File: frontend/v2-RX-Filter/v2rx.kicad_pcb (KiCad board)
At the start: 2 copper layers, 100 x 100 mm, 192 parts, among them K1 D3002, K2 D3002, K3 D3002, K4 D3002, K5 D3002, K6 D3002, K7 D3002, P1 CONN_01X02, P3 External 12V-13.8V (OSTTC0221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, P4 CONN_01X02, P5 CONN_01X02, P6 TX Filter Activate Jumper, P7 Control from MegaBasic, Q2 FDV301, Q3 RD16HHF1, Q4 FDV301, T2 OUT_TRANSF, U2 74LS145, U3 74LS145, U6 LP2951-50D

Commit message: Latest Rx updates
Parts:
- removed C83: 1000pF, HERMESLITE:C_0805
- removed C84, C85: 0.01uF, HERMESLITE:C_0805
- removed C86: 150pF, HERMESLITE:C_0805
- removed C87, C96: 1uF, HERMESLITE:C_0805
- removed C88, C89, C90, C91, C92: 0.1uF, HERMESLITE:C_0805
- removed D1, D10, D11, D12, D13, D14, D15, D16, D17, D2, D3, D4, D5, D6, D7, D8, D9: DIODE, Diodes_SMD:Diode-SMA_Standard
- removed D18: RED LED (PTT), LEDs:LED-0805
- removed K1, K2, K3, K4, K5, K6, K7: D3002, HERMESLITE:D3002
- removed L22, L32: 2.7uH, HERMESLITE:Choke_SMD_1206_Standard
- removed L23, L24, L33: 4.7uH, HERMESLITE:Choke_SMD_1206_Standard
- removed L25: 100nH, HERMESLITE:Choke_SMD_1206_Standard
- removed L26: 150nH, HERMESLITE:Choke_SMD_1206_Standard
- removed L27: 330nH, HERMESLITE:Choke_SMD_1206_Standard
- removed L28, L36: 680nH, HERMESLITE:Choke_SMD_1206_Standard
- removed L29, L37: 1.5uH, HERMESLITE:Choke_SMD_1206_Standard
- removed L30: 1uH, HERMESLITE:Choke_SMD_1206_Standard
- removed L31: 1.8uH, HERMESLITE:Choke_SMD_1206_Standard
- removed L34: 270nH, HERMESLITE:Choke_SMD_1206_Standard
- removed L35: 390nH, HERMESLITE:Choke_SMD_1206_Standard
- removed L38, L39, L40: 4700nH, HERMESLITE:Choke_SMD_1206_Standard
- removed the MH at (104.1, 53.9)
- removed the MH at (146.6, 53.8)
- removed the MH at (104.0, 92.4)
- removed the MH at (145.8, 83.4)
- removed the MH at (196.0, 54.0)
- removed the MH at (196.2, 146.2)
- removed the MH at (104.0, 146.1)
- removed MountingHole_6mm: VAL**, Mounting_Holes:MountingHole_6mm
- removed P6: TX Filter Activate Jumper, Pin_Headers:Pin_Header_Straight_1x02
- removed P7: Control from MegaBasic, Pin_Headers:Pin_Header_Straight_1x07
- removed Q2, Q4: FDV301, HERMESLITE:SOT-23-GDS
- removed Q3: RD16HHF1, Transistors_TO-220:TO-220_Neutral123_Vertical_LargePads
- removed R10: 270, HERMESLITE:R_0805
- removed R13, R14, R15, R16, R17, R18, R19: 1k, HERMESLITE:R_0805
- removed R2: 4.99k, HERMESLITE:R_0805
- removed R20, R21: 270 1W, Resistors_ThroughHole:Resistor_Vertical_RM5mm
- removed R5: 6.8, HERMESLITE:R_0805
- removed R6: 10k, HERMESLITE:R_0805
- removed T2: OUT_TRANSF, HERMESLITE:OUT_TRANSF
- removed VR1: 1k MT, Potentiometers:Potentiometer_Bourns_3296W_3-8Zoll_Inline_ScrewUp
- added C5: DNI, HERMESLITE:C_0805, F.Cu at (144.8, 136.5)
- added FB1: BLM21PG220SN1D, Resistors_SMD:R_0805_HandSoldering, F.Cu at (234.3, 129.4)
- added FB2: BLM21PG220SN1D, Resistors_SMD:R_0805_HandSoldering, F.Cu at (232.4, 140.5)
- added MH: VAL**, HERMESLITE:MH, F.Cu at (185.6, 45.0)
- added MH: VAL**, HERMESLITE:MH, F.Cu at (113.9, 45.0)
- added MH: VAL**, HERMESLITE:MH, F.Cu at (114.2, 136.2)
- added MH: VAL**, HERMESLITE:MH, F.Cu at (185.4, 136.4)
- added P2: CONN_01X02, Pin_Headers:Pin_Header_Straight_1x02, F.Cu at (205.0, 75.4)
- added U1: 4504, Housings_SOIC:SOIC-16_3.9x9.9mm_Pitch1.27mm, F.Cu at (94.7, 90.6)
- added U10: PE4259-53, HERMESLITE:sc70-6, F.Cu at (179.1, 49.8)
- added U11: PE4259-53, HERMESLITE:sc70-6, F.Cu at (178.0, 61.9)
- added U12: PE4259-53, HERMESLITE:sc70-6, F.Cu at (179.1, 76.4)
- added U13: PE4259-53, HERMESLITE:sc70-6, F.Cu at (207.8, 119.1)
- added U14: PE4259-53, HERMESLITE:sc70-6, F.Cu at (208.0, 124.7)
- added U15: PE4259-53, HERMESLITE:sc70-6, F.Cu at (208.3, 130.4)
- added U16: PE4259-53, HERMESLITE:sc70-6, F.Cu at (208.5, 136.2)
- added U4: PE4259-53, HERMESLITE:sc70-6, F.Cu at (140.1, 77.2)
- added U5: PE4259-53, HERMESLITE:sc70-6, F.Cu at (196.0, 120.5)
- added U7: PE4259-53, HERMESLITE:sc70-6, F.Cu at (196.5, 132.0)
- added U8: PE4259-53, HERMESLITE:sc70-6, F.Cu at (196.5, 137.1)
- added U9: 4504, Housings_SOIC:SOIC-16_3.9x9.9mm_Pitch1.27mm, F.Cu at (85.2, 103.8)
- C10: value 10uF 16V -> DNI; footprint Capacitors_Tantalum_SMD:TantalC_SizeB_EIA-3528_Reflow -> HERMESLITE:C_0805; moved to F.Cu
- C11: value 4700pF -> DNI; moved to F.Cu
- C12, C13: value 120pF -> DNI; moved to F.Cu
- C14: value 82pF -> DNI; moved to F.Cu
- C15, C24, C36, C38: value 150pF -> DNI; moved to F.Cu
- C16: value 150pF -> 68pF; moved to F.Cu
- C17: value 470pF -> DNI; moved to F.Cu
- C18: value 150pF -> 120pF; moved to F.Cu
- C19, C25: value 150pF -> 180pF; moved to F.Cu
- C2: value 47uF 16V -> DNI; footprint Capacitors_Tantalum_SMD:TantalC_SizeD_EIA-7343_Reflow -> HERMESLITE:C_0805; moved to F.Cu
- C20, C26: value 1800pF -> 330pF; moved to F.Cu
- C21: value DNI -> 560pF; moved to F.Cu
- C22: value DNI -> 1000pF; moved to F.Cu
- C23: value DNI -> 120pF; moved to F.Cu
- C27: value 270pF -> 560pF; moved to F.Cu
- C28: value 560pF -> 1200pF; moved to F.Cu
- C29: value 1000pF -> 1500pF; moved to F.Cu
- C3, C6: value 0.1uF -> DNI
- C30: value 3300pF -> DNI; moved to F.Cu
- C31: value 560pF -> DNI; moved to F.Cu
- C32, C33, C34: moved to F.Cu
- C35: value 220pF -> DNI; moved to F.Cu
- C37: value 3300pF -> 120pF; moved to F.Cu
- C39: value 150pF -> 270pF; moved to F.Cu
- C4, C7, C8: value 0.1uF -> DNI; moved to F.Cu
- C40: value 470pF -> 270pF; moved to F.Cu
- C41: value 150pF -> 680pF; moved to F.Cu
- C42: value 150pF -> 1200pF; moved to F.Cu
- C43: value 0.1uF -> 1500pF
- C45: value 0.01uF -> 120pF
- C46, C59, C69, C70, C71, C72: value 0.01uF -> DNI
- C47: value 0.01uF -> 180pF
- C48: value 0.01uF -> 330pF
- C49: value 100pF -> 560pF
- C50: value 270pF -> 1200pF
- C51: value 560pF -> 1500pF
- C52: value 1000pF -> 0.1uF
- C53: value 1000pF -> DNI
- C54: value 39pF -> DNI
- C55: value 56pF -> DNI
- C56, C57, C58, C67, C68, C73: value 150pF -> DNI
- C60: value 390pF -> 68pF
- C61: value 680pF -> DNI
- C62: value 1200pF -> 120pF
- C63: value 2200pF -> 180pF
- C64: value 1000pF -> 330pF
- C65: value 39pF -> 560pF
- C66: value 56pF -> 1000pF
- C74: value 270pF -> 0.1uF
- C75: value 560pF -> 0.01uF
- C76: value 1000pF -> 0.01uF
- C77, C82: value 0.1uF -> 0.01uF
- C78, C79: value 150pF -> 0.01uF
- C80, C81: value 150pF -> 0.1uF; moved to F.Cu
- C9: value 1uF -> DNI; moved to F.Cu
- L1: value FT37-43 11T #26 -> 680nH; footprint Choke_Axial_ThroughHole:Choke_Horizontal_RM10mm -> HERMESLITE:inductor
- L10: value 300nH -> 820nH; footprint Choke_Toroid_ThroughHole:Choke_Toroid_6,5x13mm_Vertical -> HERMESLITE:inductor
- L11: value 430nH -> 1.5uH; footprint Choke_Toroid_ThroughHole:Choke_Toroid_6,5x13mm_Vertical -> HERMESLITE:inductor
- L12: value 2.92uH -> 2.2uH; footprint Choke_Toroid_ThroughHole:Choke_Toroid_6,5x13mm_Vertical -> HERMESLITE:inductor
- L13: value 1.02uH -> 3.9uH; footprint Choke_Toroid_ThroughHole:Choke_Toroid_6,5x13mm_Vertical -> HERMESLITE:inductor
- L14: value 4700nH -> 8.2uH; footprint HERMESLITE:Choke_SMD_1206_Standard -> HERMESLITE:inductor
- L15: value 270nH -> 680nH; footprint HERMESLITE:Choke_SMD_1206_Standard -> HERMESLITE:inductor
- L16: value 390nH -> DNI; footprint HERMESLITE:Choke_SMD_1206_Standard -> HERMESLITE:inductor
- L17: value 680nH -> 820nH; footprint HERMESLITE:Choke_SMD_1206_Standard -> HERMESLITE:inductor
- L18: footprint HERMESLITE:Choke_SMD_1206_Standard -> HERMESLITE:inductor
- L19: value 1.5uH -> 2.2uH; footprint HERMESLITE:Choke_SMD_1206_Standard -> HERMESLITE:inductor
- L2: value 192nH -> DNI; footprint Choke_Toroid_ThroughHole:Choke_Toroid_6,5x13mm_Vertical -> HERMESLITE:inductor
- L20: value 1uH -> 3.9uH; footprint HERMESLITE:Choke_SMD_1206_Standard -> HERMESLITE:inductor
- L21: value 1.8uH -> 8.2uH; footprint HERMESLITE:Choke_SMD_1206_Standard -> HERMESLITE:inductor
- L3: value 192nH -> 820nH; footprint Choke_Toroid_ThroughHole:Choke_Toroid_6,5x13mm_Vertical -> HERMESLITE:inductor
- L4: value 240nH -> 1.5uH; footprint Choke_Toroid_ThroughHole:Choke_Toroid_6,5x13mm_Vertical -> HERMESLITE:inductor
- L5: value 300nH -> 2.2uH; footprint Choke_Toroid_ThroughHole:Choke_Toroid_6,5x13mm_Vertical -> HERMESLITE:inductor
- L6: value 430nH -> 3.9uH; footprint Choke_Toroid_ThroughHole:Choke_Toroid_6,5x13mm_Vertical -> HERMESLITE:inductor
- L7: value 1.44uH -> 8.2uH; footprint Choke_Toroid_ThroughHole:Choke_Toroid_6,5x13mm_Vertical -> HERMESLITE:inductor
- L8: value 1.02uH -> 680nH; footprint Choke_Toroid_ThroughHole:Choke_Toroid_6,5x13mm_Vertical -> HERMESLITE:inductor
- L9: value 240nH -> DNI; footprint Choke_Toroid_ThroughHole:Choke_Toroid_6,5x13mm_Vertical -> HERMESLITE:inductor
- P1: value CONN_01X02 -> CONN_02X07; footprint Pin_Headers:Pin_Header_Straight_1x02 -> Pin_Headers:Pin_Header_Straight_2x07
- P3: value External 12V-13.8V (OSTTC022162) -> CONN_02X03; footprint Connect:AK300-2 -> Pin_Headers:Pin_Header_Straight_2x03
- P4: value CONN_01X02 -> CONN_02X03; footprint Pin_Headers:Pin_Header_Straight_1x02 -> Pin_Headers:Pin_Header_Straight_2x03
- U2, U3: value 74LS145 -> PE4259-53; footprint Housings_SOIC:SOIC-16_3.9x9.9mm_Pitch1.27mm -> HERMESLITE:sc70-6
- U6: value LP2951-50D -> PE4259-53; footprint Housings_SOIC:SOIC-8_3.9x4.9mm_Pitch1.27mm -> HERMESLITE:sc70-6; moved to F.Cu
- moved C53 102.0 mm to (165.0, 49.0), turned to 270 degrees
- moved C27 90.7 mm to (121.9, 122.6), turned to 0 degrees
- moved C29 88.5 mm to (109.1, 131.4), turned to 0 degrees
- moved C33 88.5 mm to (119.4, 128.3), turned to 0 degrees
- moved C11 83.5 mm to (130.0, 143.1), turned to 0 degrees
- moved C42 82.2 mm to (109.3, 141.5), turned to 0 degrees
- moved P4 79.6 mm to (185.3, 53.4), turned to 270 degrees
- moved L4 79.4 mm to (126.2, 107.8), turned to 0 degrees
- moved C4 79.2 mm to (160.1, 136.0)
- moved L8 78.6 mm to (157.5, 51.3), turned to 0 degrees
- moved C30 77.5 mm to (157.9, 55.6), turned to 180 degrees
- moved C67 76.6 mm to (175.6, 53.8), turned to 270 degrees
- moved C8 76.3 mm to (141.9, 138.7), turned to 0 degrees
- moved C45 76.0 mm to (171.4, 56.1)
- moved C37 75.5 mm to (163.8, 52.8), turned to 180 degrees
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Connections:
- C1 pad 1: +12V -> Net-(C1-Pad1)
- C1 pad 2: GND -> Net-(C1-Pad2)
- C10 pad 2: GND -> Net-(C10-Pad2)
- C11 pad 1: GND -> Net-(C11-Pad1)
- C11 pad 2: Net-(C10-Pad1) -> Net-(C11-Pad2)
- C12 pad 2: GND -> Net-(C12-Pad2)
- C13 pad 2: GND -> Net-(C13-Pad2)
- C14 pad 1: TXIN -> Net-(C14-Pad1)
- C14 pad 2: GND -> Net-(C14-Pad2)
- C15 pad 2: GND -> Net-(C15-Pad2)
- C16 pad 2: GND -> Net-(C16-Pad2)
- C17 pad 2: GND -> Net-(C10-Pad1)
- C18 pad 2: GND -> Net-(C11-Pad1)
- C19 pad 1: Net-(C18-Pad1) -> Net-(C19-Pad1)
- C19 pad 2: GND -> Net-(C12-Pad1)
- C2 pad 1: +12V -> Net-(C2-Pad1)
- C20 pad 2: GND -> Net-(C13-Pad1)
- C21 pad 1: Net-(C15-Pad1) -> Net-(C21-Pad1)
- C21 pad 2: Net-(C21-Pad2) -> Net-(C14-Pad1)
- C22 pad 1: Net-(C16-Pad1) -> Net-(C22-Pad1)
- C22 pad 2: Net-(C22-Pad2) -> Net-(C15-Pad1)
- C23 pad 1: Net-(C17-Pad1) -> Net-(C16-Pad1)
- C23 pad 2: Net-(C23-Pad2) -> GND
- C24 pad 1: Net-(C24-Pad1) -> Net-(C17-Pad1)
- C24 pad 2: Net-(C20-Pad1) -> GND
- C25 pad 2: Net-(C25-Pad2) -> GND
- C26 pad 1: Net-(C24-Pad1) -> Net-(C19-Pad1)
- C27 pad 1: Net-(C21-Pad2) -> Net-(C20-Pad1)
- C28 pad 1: Net-(C22-Pad2) -> Net-(C21-Pad1)
- C29 pad 1: Net-(C23-Pad2) -> Net-(C22-Pad1)
- C3 pad 1: Net-(C3-Pad1) -> Net-(C10-Pad2)
- C3 pad 2: Net-(C3-Pad2) -> GND
- C30 pad 2: GND -> Net-(C16-Pad1)
- C31 pad 1: Net-(C25-Pad2) -> Net-(C31-Pad1)
- C31 pad 2: GND -> Net-(C17-Pad1)
- C32 pad 1: Net-(C21-Pad2) -> Net-(C32-Pad1)
- C32 pad 2: Net-(C32-Pad2) -> Net-(C18-Pad1)
- C33 pad 1: Net-(C22-Pad2) -> Net-(C33-Pad1)
- C33 pad 2: Net-(C33-Pad2) -> Net-(C19-Pad1)
- C34 pad 1: Net-(C23-Pad2) -> Net-(C34-Pad1)
- C34 pad 2: Net-(C34-Pad2) -> Net-(C20-Pad1)
- C35 pad 2: Net-(C30-Pad1) -> Net-(C21-Pad1)
- C36 pad 1: Net-(C25-Pad2) -> Net-(C36-Pad1)
- C36 pad 2: Net-(C36-Pad2) -> Net-(C22-Pad1)
- C37 pad 1: Net-(C35-Pad1) -> Net-(C37-Pad1)
- C37 pad 2: GND -> Net-(C30-Pad1)
- C38 pad 1: Net-(C32-Pad2) -> Net-(C38-Pad1)
- C38 pad 2: GND -> Net-(C31-Pad1)
- C39 pad 1: Net-(C33-Pad2) -> Net-(C39-Pad1)
- C39 pad 2: GND -> Net-(C32-Pad1)
- C4 pad 1: Net-(C4-Pad1) -> Net-(C11-Pad2)
- C40 pad 1: Net-(C34-Pad2) -> Net-(C40-Pad1)
- C40 pad 2: GND -> Net-(C33-Pad1)
- C41 pad 1: Net-(C36-Pad2) -> Net-(C41-Pad1)
- C41 pad 2: GND -> Net-(C34-Pad1)
- C42 pad 1: Net-(C36-Pad2) -> Net-(C42-Pad1)
- C42 pad 2: GND -> Net-(C35-Pad1)
- C43 pad 2: RX-OUT -> Net-(C36-Pad1)
- C44 pad 1: Net-(C44-Pad1) -> GND
- C44 pad 2: GND -> Net-(C44-Pad2)
- C45 pad 1: Net-(C45-Pad1) -> Net-(C37-Pad1)
- C46 pad 1: Net-(C46-Pad1) -> Net-(C38-Pad1)
- C47 pad 1: Net-(C47-Pad1) -> Net-(C39-Pad1)
- C48 pad 1: Net-(C48-Pad1) -> Net-(C40-Pad1)
- C49 pad 1: Net-(C49-Pad1) -> Net-(C41-Pad1)
- C50 pad 1: Net-(C50-Pad1) -> Net-(C42-Pad1)
- C51 pad 1: Net-(C51-Pad1) -> Net-(C43-Pad1)
- C53 pad 2: GND -> Net-(C37-Pad1)
- C54 pad 2: Net-(C54-Pad2) -> Net-(C38-Pad1)
- C55 pad 2: Net-(C55-Pad2) -> Net-(C39-Pad1)
- C56 pad 2: Net-(C56-Pad2) -> Net-(C40-Pad1)
- C57 pad 2: Net-(C57-Pad2) -> Net-(C41-Pad1)
- C58 pad 2: Net-(C58-Pad2) -> Net-(C42-Pad1)
- C59 pad 1: Net-(C48-Pad1) -> Net-(C59-Pad1)
- C59 pad 2: GND -> Net-(C43-Pad1)
- C6 pad 1: Net-(C6-Pad1) -> Net-(C13-Pad2)
- C6 pad 2: Net-(C6-Pad2) -> GND
- C60 pad 1: Net-(C54-Pad1) -> Net-(C60-Pad1)
- C60 pad 2: GND -> Net-(C53-Pad1)
- C61 pad 1: Net-(C55-Pad1) -> Net-(C61-Pad1)
- C61 pad 2: GND -> Net-(C54-Pad1)
- C62 pad 1: Net-(C56-Pad1) -> Net-(C62-Pad1)
- C62 pad 2: GND -> Net-(C55-Pad1)
- C63 pad 1: Net-(C57-Pad1) -> Net-(C63-Pad1)
- C63 pad 2: GND -> Net-(C56-Pad1)
- C64 pad 1: Net-(C58-Pad1) -> Net-(C64-Pad1)
- C64 pad 2: GND -> Net-(C57-Pad1)
- C65 pad 2: Net-(C65-Pad2) -> Net-(C58-Pad1)
- C66 pad 2: Net-(C66-Pad2) -> Net-(C59-Pad1)
- C67 pad 1: Net-(C67-Pad1) -> Net-(C60-Pad1)
- C67 pad 2: Net-(C67-Pad2) -> GND
- C68 pad 1: Net-(C68-Pad1) -> Net-(C61-Pad1)
- C68 pad 2: Net-(C68-Pad2) -> GND
- C69 pad 1: Net-(C44-Pad1) -> Net-(C62-Pad1)
- C7 pad 1: GND -> Net-(C14-Pad2)
- C7 pad 2: Net-(C10-Pad1) -> GND
- C70 pad 1: Net-(C45-Pad1) -> Net-(C63-Pad1)
- C71 pad 1: Net-(C46-Pad1) -> Net-(C64-Pad1)
- C72 pad 1: Net-(C47-Pad1) -> Net-(C65-Pad1)
- C73 pad 1: Net-(C65-Pad1) -> Net-(C66-Pad1)
- C74 pad 1: Net-(C66-Pad1) -> Net-(C74-Pad1)
- C74 pad 2: GND -> Net-(C74-Pad2)
- C75 pad 1: Net-(C67-Pad1) -> GND
- C75 pad 2: GND -> Net-(C75-Pad2)
- C76 pad 1: Net-(C68-Pad1) -> GND
- C76 pad 2: GND -> Net-(C76-Pad2)
- C77 pad 1: RX-IN -> GND
- C78 pad 1: Net-(C57-Pad1) -> GND
- C78 pad 2: Net-(C57-Pad2) -> Net-(C78-Pad2)
- C79 pad 1: Net-(C68-Pad1) -> GND
- C79 pad 2: Net-(C68-Pad2) -> Net-(C79-Pad2)
- C8 pad 1: GND -> Net-(C15-Pad2)
- C8 pad 2: Net-(C10-Pad1) -> GND
- C80 pad 1: Net-(C16-Pad1) -> Net-(C52-Pad1)
- C81 pad 1: Net-(C33-Pad2) -> GND
- C81 pad 2: GND -> Net-(C81-Pad2)
- C82 pad 1: Net-(C82-Pad1) -> GND
- C82 pad 2: TXIN -> Net-(C82-Pad2)
- C9 pad 1: GND -> Net-(C16-Pad2)
- C9 pad 2: Net-(C10-Pad1) -> Net-(C2-Pad1)
- L1 pad 1: +12V -> Net-(C2-Pad1)
- L1 pad 2: Net-(C10-Pad1) -> Net-(C16-Pad2)
- L10 pad 1: Net-(C22-Pad2) -> Net-(C18-Pad1)
- L10 pad 2: Net-(C33-Pad2) -> Net-(C32-Pad1)
- L11 pad 1: Net-(C23-Pad2) -> Net-(C19-Pad1)
- L11 pad 2: Net-(C34-Pad2) -> Net-(C33-Pad1)
- L12 pad 1: Net-(C30-Pad1) -> Net-(C20-Pad1)
- L12 pad 2: Net-(C35-Pad1) -> Net-(C34-Pad1)
- L13 pad 1: Net-(C25-Pad2) -> Net-(C21-Pad1)
- L13 pad 2: Net-(C36-Pad2) -> Net-(C35-Pad1)
- L14 pad 1: Net-(L14-Pad1) -> Net-(C22-Pad1)
- L14 pad 2: Net-(C43-Pad1) -> Net-(C36-Pad1)
- L15 pad 1: Net-(C49-Pad1) -> Net-(C37-Pad1)
- L15 pad 2: Net-(C44-Pad1) -> Net-(C53-Pad1)
- L16 pad 1: Net-(C50-Pad1) -> Net-(C38-Pad1)
- L16 pad 2: Net-(C45-Pad1) -> Net-(C54-Pad1)
- L17 pad 1: Net-(C51-Pad1) -> Net-(C39-Pad1)
- L17 pad 2: Net-(C46-Pad1) -> Net-(C55-Pad1)
- L18 pad 1: Net-(C52-Pad1) -> Net-(C40-Pad1)
- L18 pad 2: Net-(C47-Pad1) -> Net-(C56-Pad1)
- L19 pad 1: Net-(C53-Pad1) -> Net-(C41-Pad1)
- L19 pad 2: Net-(C48-Pad1) -> Net-(C57-Pad1)
- L2 pad 1: Net-(C13-Pad1) -> Net-(C10-Pad2)
- L2 pad 2: Net-(C12-Pad1) -> Net-(C10-Pad1)
- L20 pad 1: Net-(C49-Pad1) -> Net-(C42-Pad1)
- L20 pad 2: Net-(C54-Pad2) -> Net-(C58-Pad1)
- L21 pad 1: Net-(C50-Pad1) -> Net-(C43-Pad1)
- L21 pad 2: Net-(C55-Pad2) -> Net-(C59-Pad1)
- L3 pad 1: TXIN -> Net-(C11-Pad2)
- L3 pad 2: Net-(C13-Pad1) -> Net-(C11-Pad1)
- L4 pad 1: Net-(C15-Pad1) -> Net-(C12-Pad2)
- L4 pad 2: Net-(C21-Pad2) -> Net-(C12-Pad1)
- L5 pad 1: Net-(C16-Pad1) -> Net-(C13-Pad2)
- L5 pad 2: Net-(C22-Pad2) -> Net-(C13-Pad1)
- L6 pad 1: Net-(C17-Pad1) -> Net-(C14-Pad2)
- L6 pad 2: Net-(C23-Pad2) -> Net-(C14-Pad1)
- L7 pad 1: Net-(C20-Pad1) -> Net-(C15-Pad2)
- L7 pad 2: Net-(C24-Pad1) -> Net-(C15-Pad1)
- L8 pad 1: Net-(C18-Pad1) -> Net-(C16-Pad1)
- L8 pad 2: Net-(C25-Pad2) -> Net-(C30-Pad1)
- L9 pad 1: Net-(C21-Pad2) -> Net-(C17-Pad1)
- L9 pad 2: Net-(C32-Pad2) -> Net-(C31-Pad1)
- P1 pad 1: GND -> Net-(P1-Pad1)
- P1 pad 2: Net-(K1-Pad3) -> GND
- P3 pad 1: GND -> Net-(P3-Pad1)
- P3 pad 2: +12V -> GND
- P4 pad 1: GND -> Net-(P4-Pad1)
- P4 pad 2: Net-(C3-Pad2) -> GND
- P5 pad 2: RX-OUT -> Net-(C74-Pad1)
- U2 pad 1: Net-(K7-Pad10) -> Net-(P3-Pad1)
- U2 pad 2: Net-(K6-Pad10) -> GND
- U2 pad 3: Net-(K5-Pad10) -> Net-(P3-Pad5)
- U2 pad 4: Net-(K5-Pad10) -> Net-(C44-Pad2)
- U2 pad 5: Net-(K4-Pad10) -> Net-(C2-Pad1)
- U2 pad 6: Net-(K4-Pad10) -> Net-(C81-Pad2)
- U3 pad 1: Net-(C48-Pad1) -> GND
- U3 pad 2: Net-(C47-Pad1) -> GND
- U3 pad 3: Net-(C47-Pad1) -> Net-(C1-Pad1)
- U3 pad 4: Net-(C46-Pad1) -> Net-(C75-Pad2)
- U3 pad 5: Net-(C46-Pad1) -> Net-(C10-Pad2)
- U3 pad 6: Net-(C45-Pad1) -> Net-(C81-Pad2)
- U6 pad 1: 5V -> GND
- U6 pad 2: 5V -> GND
- U6 pad 3: GND -> Net-(C1-Pad1)
- U6 pad 4: GND -> Net-(C78-Pad2)
- U6 pad 5: Net-(U6-Pad5) -> Net-(C13-Pad2)
- U6 pad 6: Net-(U6-Pad6) -> Net-(C81-Pad2)
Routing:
- net +12V: track 328.3 -> 0.00 mm, vias 10 -> 0
- net GND: track 203.5 -> 23.3 mm, vias 61 -> 9
- net Net-(K2-Pad1): track 117.4 -> 0.00 mm, vias 1 -> 0
- net 5V: track 86.1 -> 0.00 mm, vias 2 -> 0
- net Net-(P7-Pad2): track 85.7 -> 0.00 mm, vias 5 -> 0
- net Net-(C47-Pad1): track 76.3 -> 0.00 mm, vias 4 -> 0
- net Net-(C46-Pad1): track 75.2 -> 0.00 mm, vias 3 -> 0
- net Net-(D1-Pad1): track 75.0 -> 0.00 mm
- net Net-(K1-Pad7): track 72.9 -> 0.00 mm, vias 3 -> 0
- net Net-(C45-Pad1): track 69.7 -> 0.00 mm, vias 2 -> 0
- net Net-(C44-Pad1): track 68.5 -> 0.00 mm, vias 3 -> 0
- net Net-(C48-Pad1): track 68.5 -> 0.00 mm
- net Net-(C81-Pad2): track 0.00 -> 67.1 mm, vias 0 -> 4
- net Net-(K2-Pad10): track 64.4 -> 0.00 mm, vias 2 -> 0
- net Net-(C6-Pad2): track 59.9 -> 0.00 mm
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- removed copper zone on F.Cu, net GND
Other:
- board size 100 x 100 mm -> 80 x 101.2 mm
- board text removed: "+12-14V"
- board text removed: "ANT"
- board text removed: "GND"
- board text removed: "RX"
- board text removed: "Shield"
- board text removed: "TX"

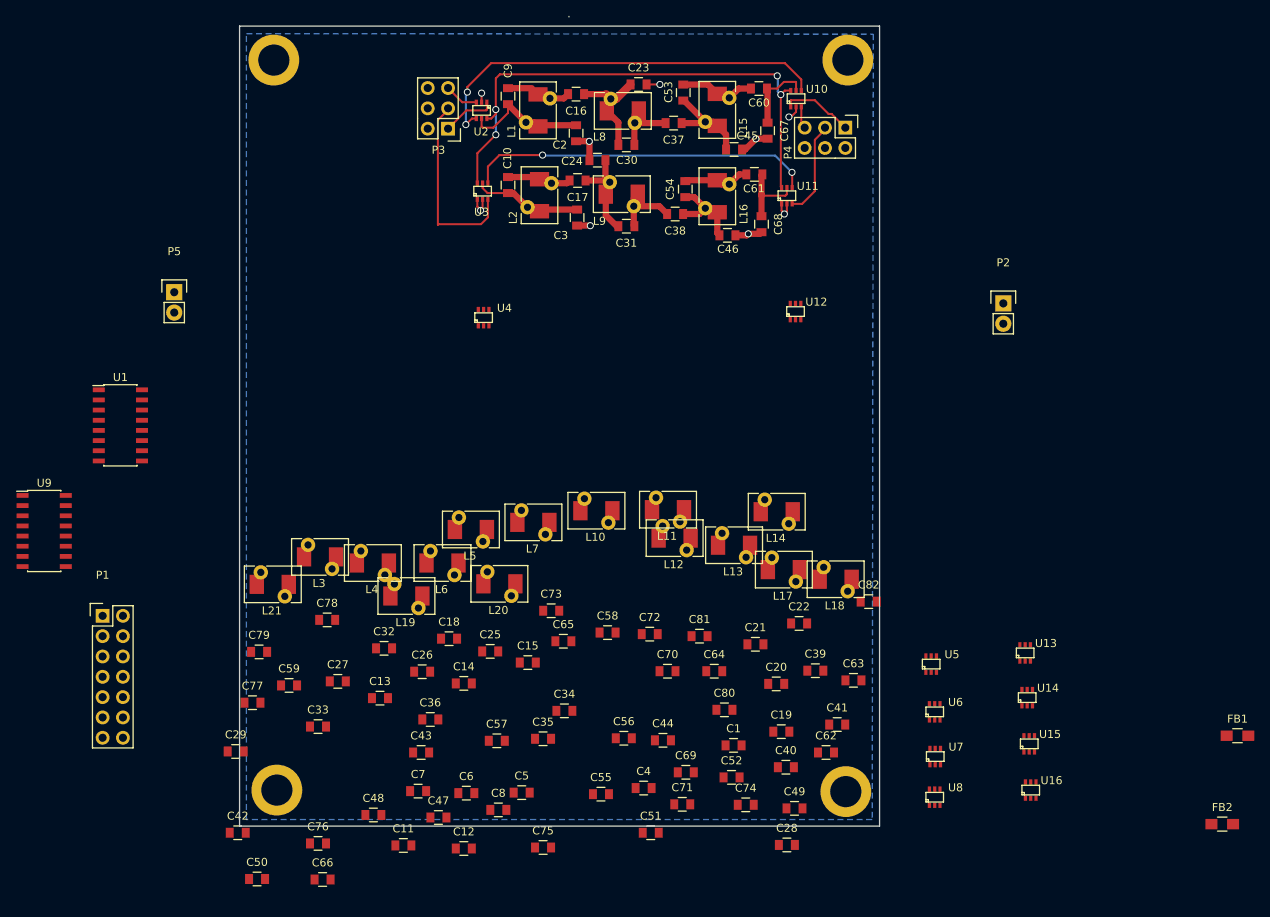
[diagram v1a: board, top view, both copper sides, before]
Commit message: New RX Filter Board Layout
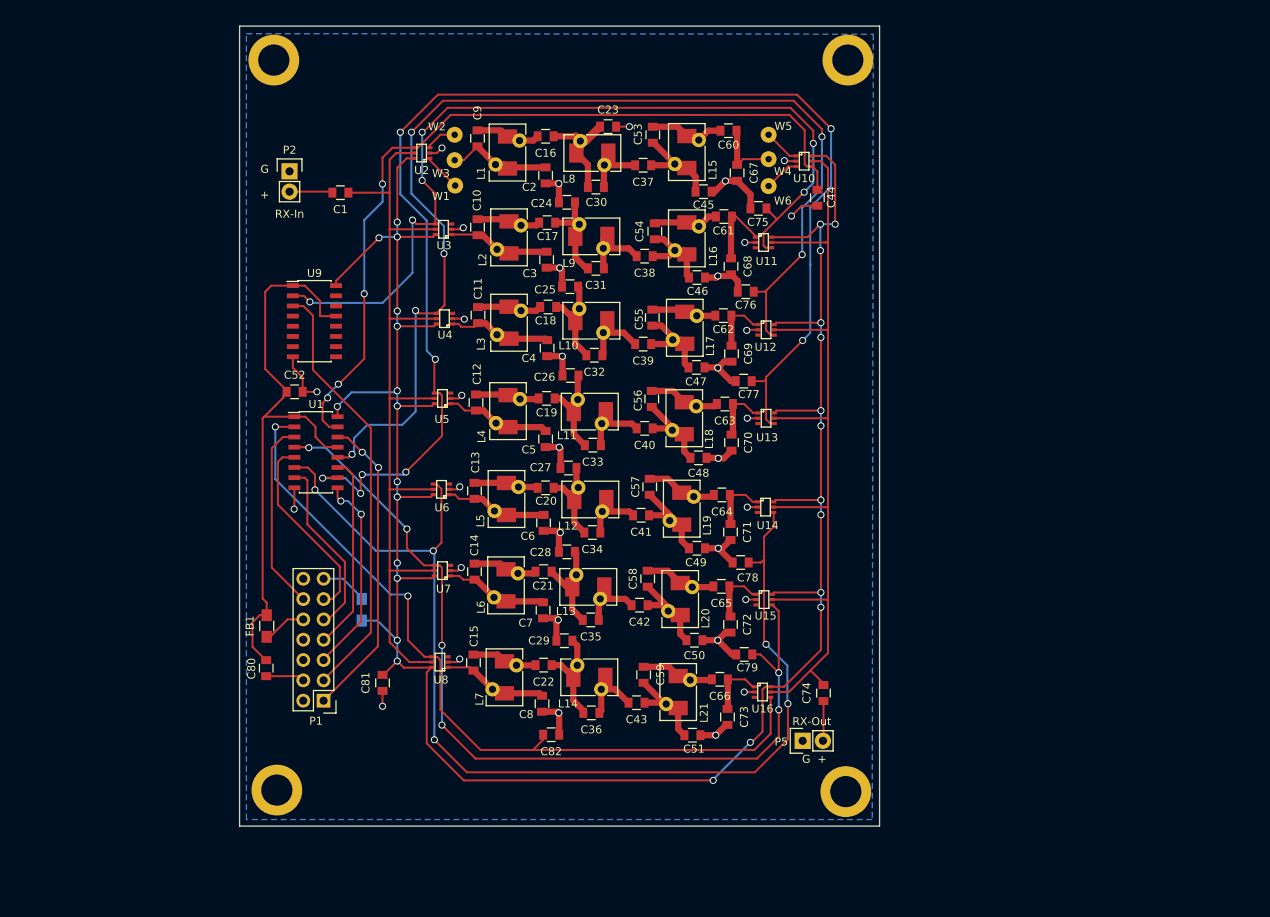
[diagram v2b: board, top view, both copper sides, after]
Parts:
- removed P3, P4: CONN_02X03, Pin_Headers:Pin_Header_Straight_2x03
- added W1: TEST_1P, Wire_Pads:SolderWirePad_single_0-8mmDrill, F.Cu at (136.5, 60.6)
- added W2: TEST_1P, Wire_Pads:SolderWirePad_single_0-8mmDrill, F.Cu at (136.5, 54.3)
- added W3: TEST_1P, Wire_Pads:SolderWirePad_single_0-8mmDrill, F.Cu at (136.5, 57.5)
- added W4: TEST_1P, Wire_Pads:SolderWirePad_single_0-8mmDrill, F.Cu at (175.7, 57.3)
- added W5: TEST_1P, Wire_Pads:SolderWirePad_single_0-8mmDrill, F.Cu at (175.7, 54.3)
- added W6: TEST_1P, Wire_Pads:SolderWirePad_single_0-8mmDrill, F.Cu at (175.7, 60.7)
- FB2: moved to B.Cu
- moved FB1 122.1 mm to (113.0, 115.7), turned to 90 degrees
- moved FB2 110.9 mm to (124.8, 113.7), turned to 270 degrees
- moved P5 96.5 mm to (180.0, 130.0), turned to 90 degrees
- moved P2 90.7 mm to (115.8, 58.9)
- moved C76 87.3 mm to (172.8, 73.9)
- moved C1 84.8 mm to (122.2, 61.5), turned to 180 degrees
- moved C75 84.3 mm to (174.4, 63.5)
- moved C77 73.4 mm to (172.6, 85.1)
- moved C52 72.8 mm to (116.5, 86.4)
- moved C44 70.5 mm to (181.8, 62.2), turned to 90 degrees
- moved U5 69.5 mm to (134.9, 87.2), turned to 90 degrees
- moved U6 67.6 mm to (134.8, 98.6), turned to 90 degrees
- moved C11 66.9 mm to (139.4, 76.8), turned to 270 degrees
- moved U7 65.8 mm to (134.9, 108.8), turned to 90 degrees
- moved C47 64.9 mm to (166.7, 83.4)
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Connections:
- U10 pad 5: Net-(C60-Pad1) -> Net-(C74-Pad2)
- U11 pad 1: GND -> Net-(C61-Pad1)
- U11 pad 3: Net-(C74-Pad2) -> Net-(U11-Pad3)
- U11 pad 5: Net-(C61-Pad1) -> Net-(C74-Pad2)
- U12 pad 1: GND -> Net-(C62-Pad1)
- U12 pad 3: Net-(C74-Pad2) -> Net-(U12-Pad3)
- U12 pad 5: Net-(C62-Pad1) -> Net-(C74-Pad2)
- U13 pad 1: GND -> Net-(C63-Pad1)
- U13 pad 3: Net-(C74-Pad2) -> Net-(U13-Pad3)
- U13 pad 5: Net-(C63-Pad1) -> Net-(C74-Pad2)
- U14 pad 1: GND -> Net-(C64-Pad1)
- U14 pad 3: Net-(C74-Pad2) -> Net-(U14-Pad3)
- U14 pad 5: Net-(C64-Pad1) -> Net-(C74-Pad2)
- U15 pad 1: GND -> Net-(C65-Pad1)
- U15 pad 3: Net-(C74-Pad2) -> Net-(U15-Pad3)
- U15 pad 5: Net-(C65-Pad1) -> Net-(C74-Pad2)
- U16 pad 1: GND -> Net-(C66-Pad1)
- U16 pad 3: Net-(C74-Pad2) -> Net-(U16-Pad3)
- U16 pad 5: Net-(C66-Pad1) -> Net-(C74-Pad2)
- U2 pad 5: Net-(C2-Pad1) -> Net-(C1-Pad1)
- U3 pad 1: GND -> Net-(C10-Pad2)
- U3 pad 3: Net-(C1-Pad1) -> Net-(U3-Pad3)
- U3 pad 5: Net-(C10-Pad2) -> Net-(C1-Pad1)
- U4 pad 1: GND -> Net-(C11-Pad2)
- U4 pad 3: Net-(C1-Pad1) -> Net-(U4-Pad3)
- U4 pad 5: Net-(C11-Pad2) -> Net-(C1-Pad1)
- U5 pad 1: GND -> Net-(C12-Pad2)
- U5 pad 3: Net-(C1-Pad1) -> Net-(U5-Pad3)
- U5 pad 5: Net-(C12-Pad2) -> Net-(C1-Pad1)
- U6 pad 1: GND -> Net-(C13-Pad2)
- U6 pad 3: Net-(C1-Pad1) -> Net-(U6-Pad3)
- U6 pad 5: Net-(C13-Pad2) -> Net-(C1-Pad1)
- U7 pad 1: GND -> Net-(C14-Pad2)
- U7 pad 3: Net-(C1-Pad1) -> Net-(U7-Pad3)
- U7 pad 5: Net-(C14-Pad2) -> Net-(C1-Pad1)
- U8 pad 1: GND -> Net-(C15-Pad2)
- U8 pad 3: Net-(C1-Pad1) -> Net-(U8-Pad3)
- U8 pad 5: Net-(C15-Pad2) -> Net-(C1-Pad1)
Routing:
- net Net-(C81-Pad2): track 67.1 -> 288.6 mm, vias 4 -> 27
- net Net-(C77-Pad2): track 0.00 -> 162.9 mm, vias 0 -> 8
- net Net-(C76-Pad2): track 0.00 -> 138.6 mm, vias 0 -> 6
- net Net-(C78-Pad2): track 0.00 -> 135.7 mm, vias 0 -> 5
- net Net-(C79-Pad2): track 0.00 -> 111.9 mm, vias 0 -> 6
- net Net-(C82-Pad2): track 0.00 -> 99.6 mm, vias 0 -> 2
- net Net-(C74-Pad2): track 12.0 -> 109.7 mm
- net GND: track 23.3 -> 114.3 mm, vias 9 -> 33
- net Net-(C1-Pad1): track 24.0 -> 103.6 mm
- net Net-(C52-Pad1): track 0.00 -> 74.0 mm
- net Net-(C75-Pad2): track 43.5 -> 110.0 mm, vias 2 -> 6
- net Net-(P1-Pad3): track 0.00 -> 54.0 mm
- net Net-(C44-Pad2): track 51.6 -> 102.5 mm, vias 2 -> 4
- net Net-(P1-Pad1): track 0.00 -> 38.7 mm, vias 0 -> 2
- net Net-(P1-Pad5): track 0.00 -> 25.2 mm, vias 0 -> 2
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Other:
- board size 80 x 101.2 mm -> 80 x 100 mm
- board text added: "G +"
- board text added: "Hermes Lite Pre-V2 RX Filter Board © W9JSW 2016 Ver 1.0"
- board text added: "RX-In"
- board text added: "RX-Out"
- board text removed: "Hermes Lite Megaband Power Amplifier © AC9HY/WA2EUJ 2015 Ver 1.2"

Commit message: Added additional bypass caps
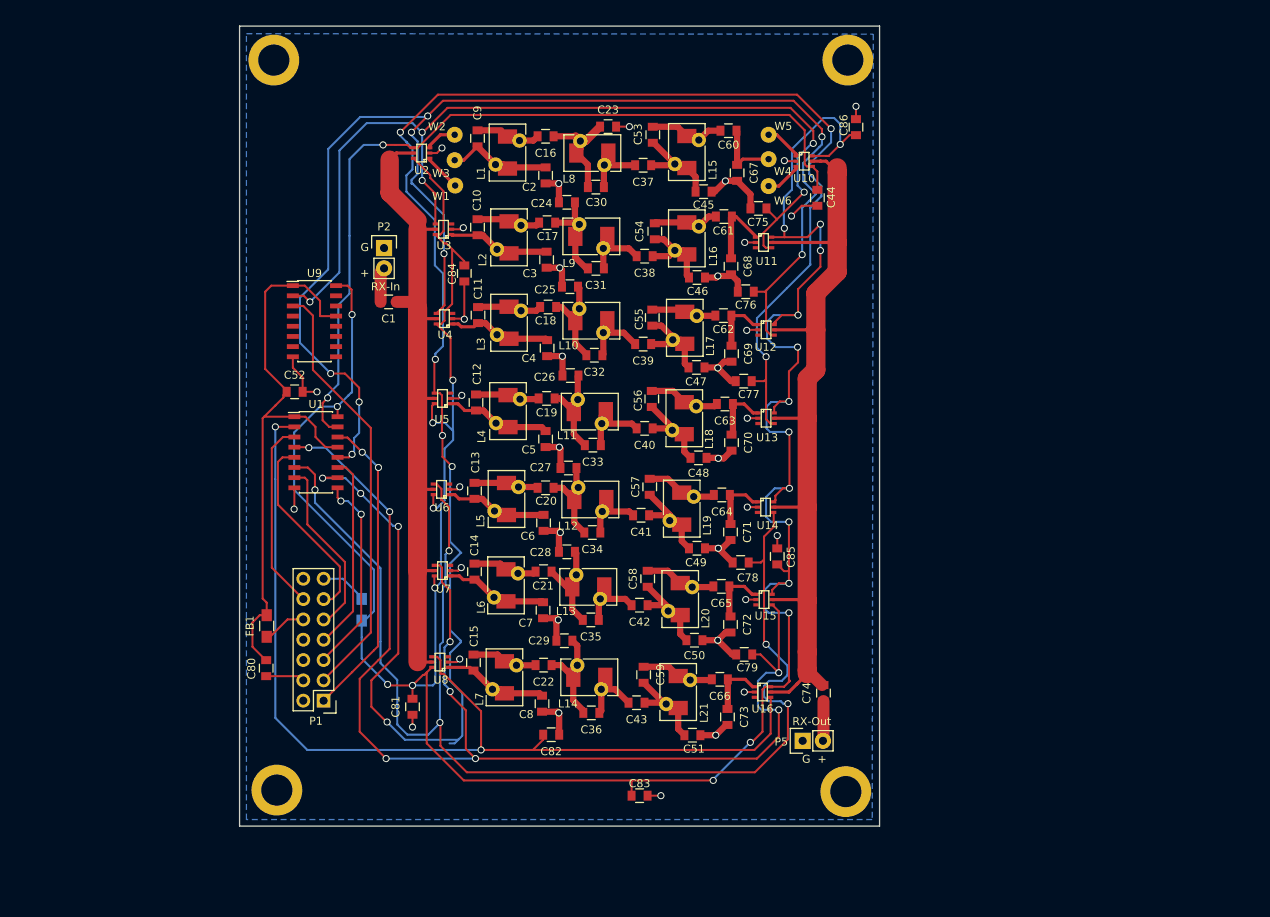
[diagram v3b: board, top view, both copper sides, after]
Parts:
- added C83: 0.01uF, HERMESLITE:C_0805, F.Cu at (159.6, 136.9)
- added C84: 0.01uF, HERMESLITE:C_0805, F.Cu at (137.7, 71.6)
- added C85: 0.01uF, HERMESLITE:C_0805, F.Cu at (176.8, 107.0)
- added C86: 0.01uF, HERMESLITE:C_0805, F.Cu at (186.6, 53.3)
- moved P2 15.2 mm to (127.6, 68.5)
- moved C1 14.9 mm to (128.2, 75.2)
- moved C81 4.79 mm to (131.2, 125.8)
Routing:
- net Net-(C77-Pad2): track 162.9 -> 238.2 mm, vias 8 -> 10
- net Net-(C81-Pad2): track 288.6 -> 357.2 mm, vias 27 -> 22
- net Net-(C79-Pad2): track 111.9 -> 152.4 mm, vias 6 -> 8
- net Net-(C76-Pad2): track 138.6 -> 172.3 mm, vias 6 -> 8
- net Net-(C78-Pad2): track 135.7 -> 162.7 mm
- net Net-(C82-Pad2): track 99.6 -> 125.0 mm
- net Net-(C1-Pad1): track 103.6 -> 84.1 mm
- net Net-(C75-Pad2): track 110.0 -> 119.6 mm, vias 6 -> 5
- net GND: track 114.3 -> 123.5 mm, vias 33 -> 36
- net Net-(C74-Pad2): track 109.7 -> 112.8 mm
- net Net-(C44-Pad2): track 102.5 -> 105.0 mm, vias 4 -> 2
- net Net-(C1-Pad2): track 5.40 -> 4.37 mm
